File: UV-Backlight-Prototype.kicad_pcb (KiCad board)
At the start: 2 copper layers, 100 x 100 mm, 86 parts, among them J1 Conn_02x08_Odd_Even

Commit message: Progress Update
Changes to PCB:
Adjusted LED placement
Started Test point placement

Changes to schematic:
Test points for VCC and GND for LED strings 1,2,3 deemed redundant and removed.
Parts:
- removed JP1, JP10, JP11, JP12, JP13, JP14, JP15, JP17, JP18, JP19, JP2, JP20, JP21, JP22, JP23, JP3, JP4, JP5, JP6, JP7, JP9: Jumper_2_Open, Resistor_SMD:R_1206_3216Metric_Pad1.30x1.75mm_HandSolder
- JP16: renamed from LEDS 2
- JP24: renamed from LEDS 3
- JP8: renamed from LEDS 1
- moved D21 178.7 mm to (195.1, 95.1), turned to 180 degrees
- moved D14 175.4 mm to (195.1, 80.1), turned to 180 degrees
- moved D7 173.5 mm to (195.1, 65.1), turned to 180 degrees
- moved D20 172.0 mm to (180.1, 95.1), turned to 180 degrees
- moved D13 168.6 mm to (180.1, 80.1), turned to 180 degrees
- moved D6 166.6 mm to (180.1, 65.1), turned to 180 degrees
- moved D19 165.6 mm to (165.1, 95.1), turned to 180 degrees
- moved D12 162.1 mm to (165.1, 80.1), turned to 180 degrees
- moved D5 160.0 mm to (165.1, 65.1), turned to 180 degrees
- moved D18 159.4 mm to (150.1, 95.1), turned to 180 degrees
- moved D11 155.8 mm to (150.1, 80.1), turned to 180 degrees
- moved D17 154.2 mm to (135.1, 95.1), turned to 180 degrees
- moved D4 153.6 mm to (150.1, 65.1), turned to 180 degrees
- moved D10 149.7 mm to (135.1, 80.1), turned to 180 degrees
- moved D16 148.5 mm to (120.1, 95.1), turned to 180 degrees
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
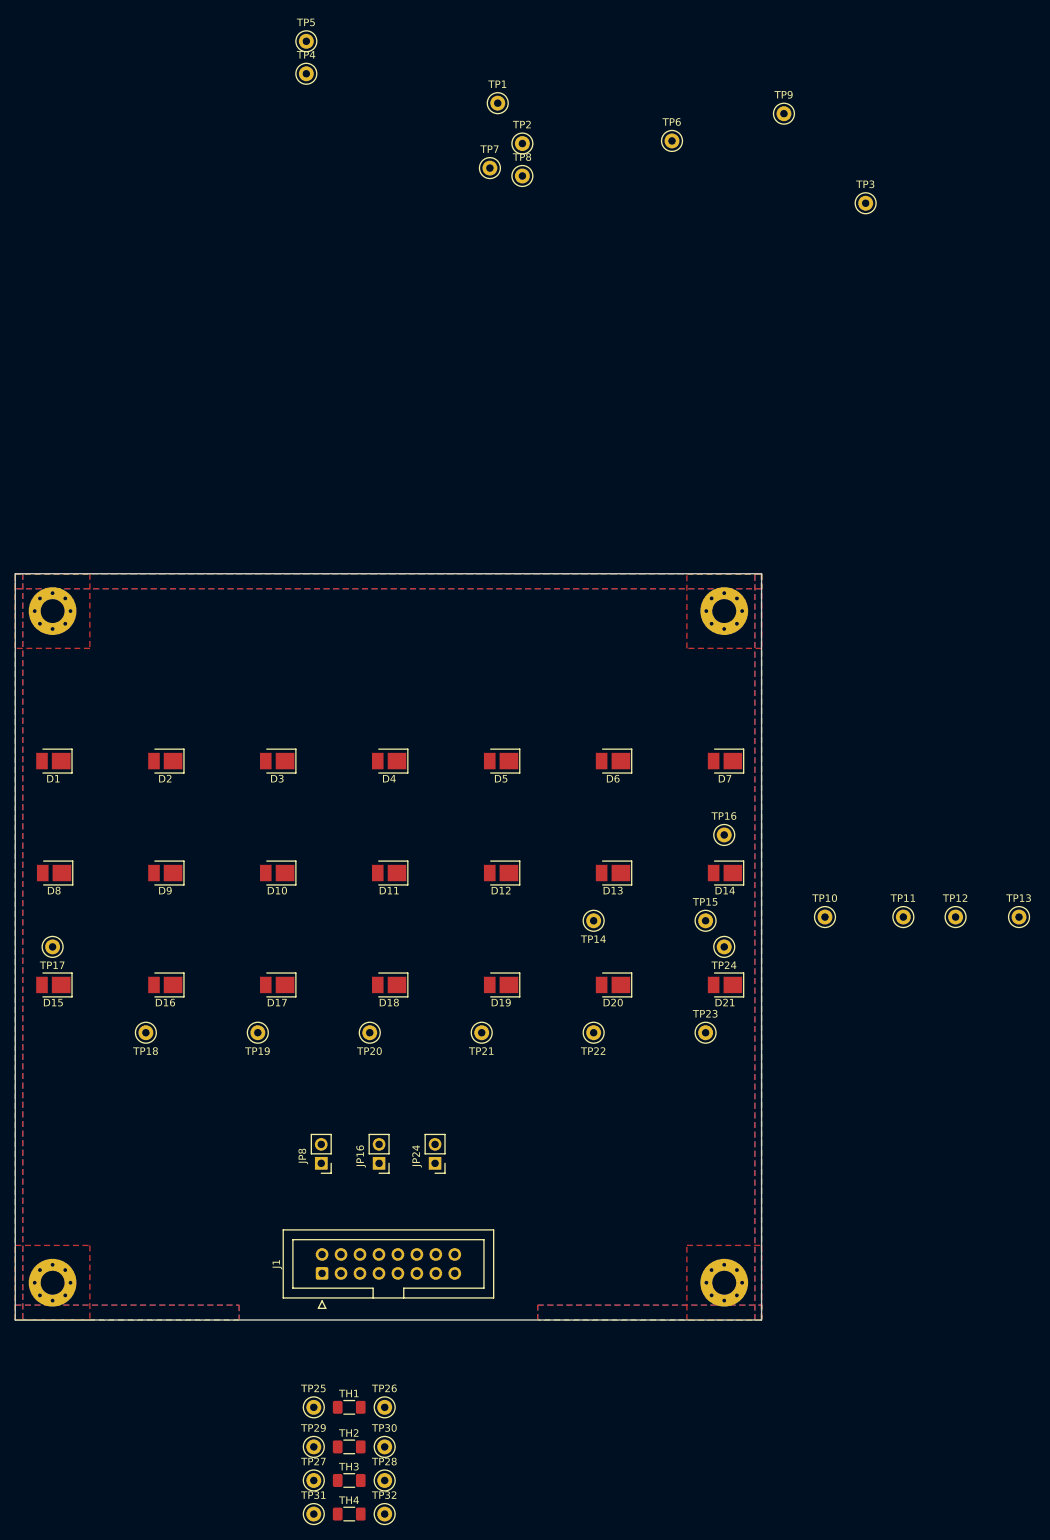
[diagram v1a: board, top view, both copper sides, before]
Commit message: PCB
Component placement complete
Added a section for testpoints for only the thermistors.

Open space bottom right - Add perfboard for prototyping CC drivers
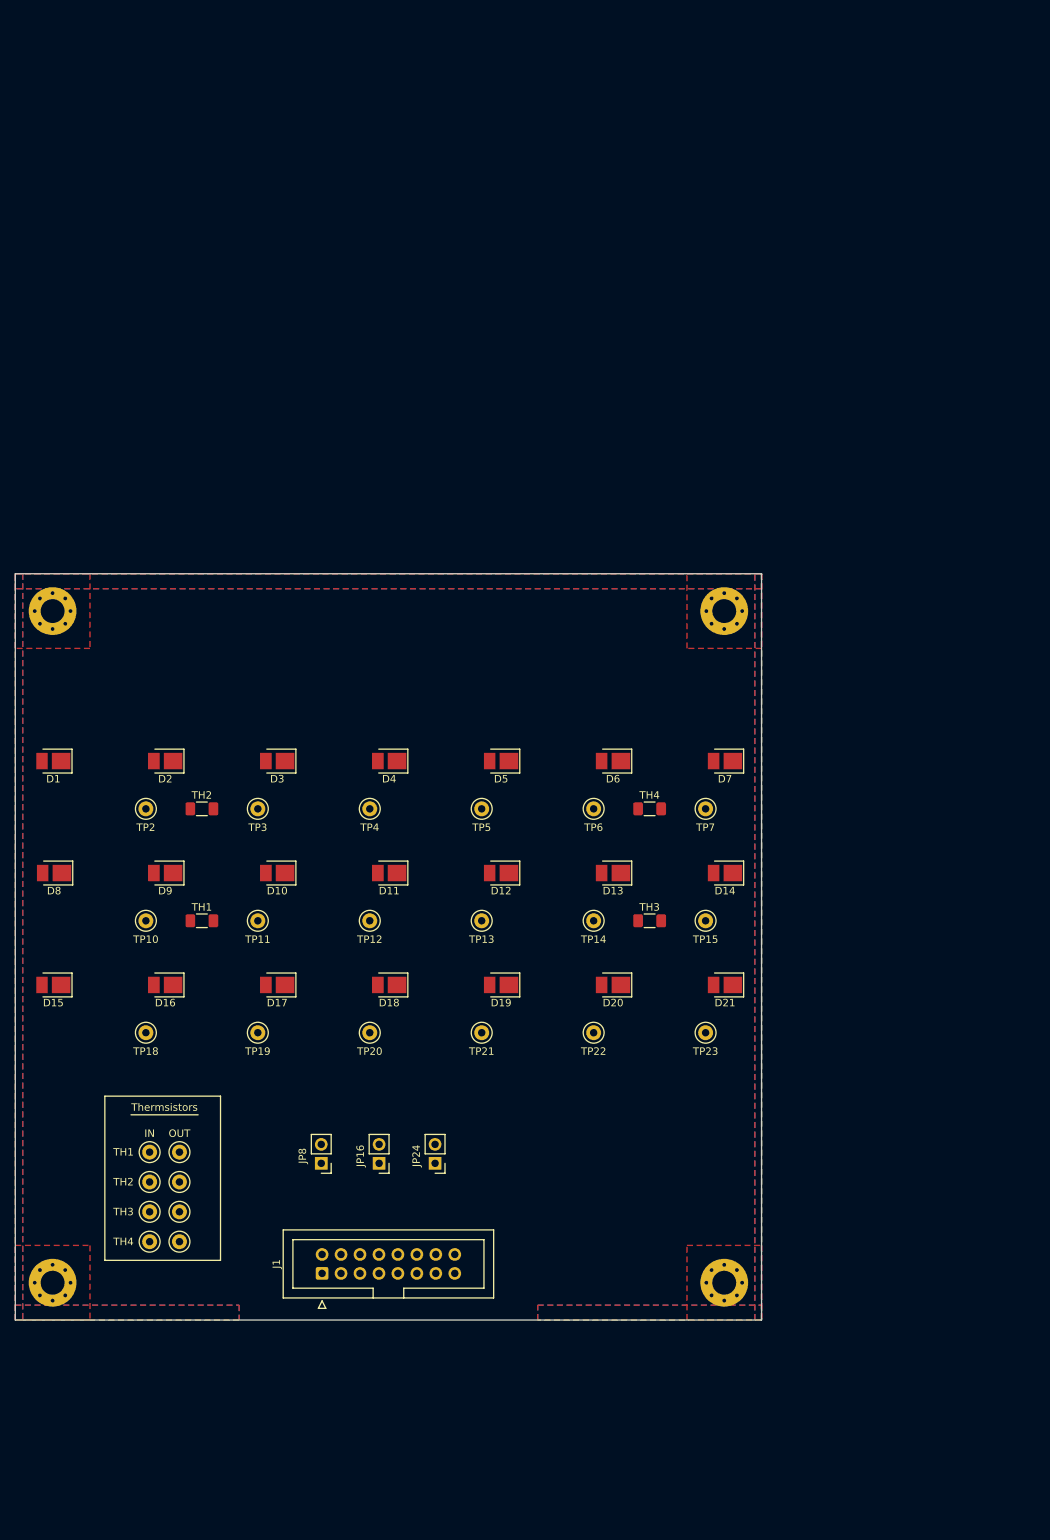
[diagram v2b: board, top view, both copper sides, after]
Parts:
- removed TP1: +LED1, TestPoint:TestPoint_Keystone_5000-5004_Miniature
- removed TP16: -LED14, TestPoint:TestPoint_Keystone_5000-5004_Miniature
- removed TP17: +LED15, TestPoint:TestPoint_Keystone_5000-5004_Miniature
- removed TP24: -LED21, TestPoint:TestPoint_Keystone_5000-5004_Miniature
- removed TP8: -LED7, TestPoint:TestPoint_Keystone_5000-5004_Miniature
- removed TP9: +LED8, TestPoint:TestPoint_Keystone_5000-5004_Miniature
- moved TP3 115.0 mm to (132.5, 71.5)
- moved TP5 105.5 mm to (162.5, 71.5)
- moved TH4 102.7 mm to (185.0, 71.5)
- moved TP2 102.4 mm to (117.5, 71.5)
- moved TP4 98.9 mm to (147.5, 71.5)
- moved TP10 91.0 mm to (117.5, 86.5)
- moved TP7 90.6 mm to (192.5, 71.5)
- moved TP6 90.1 mm to (177.5, 71.5)
- moved TH2 87.8 mm to (125.0, 71.5)
- moved TP11 86.5 mm to (132.5, 86.5)
- moved TH3 85.1 mm to (185.0, 86.5)
- moved TP12 78.5 mm to (147.5, 86.5)
- moved TP13 72.0 mm to (162.5, 86.5)
- moved TH1 68.1 mm to (125.0, 86.5)
- moved TP32 45.7 mm to (122.0, 129.5)
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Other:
- board text added: "IN"
- board text added: "OUT"
- board text added: "TH1"
- board text added: "TH2"
- board text added: "TH3"
- board text added: "TH4"
- board text added: "Thermsistors"

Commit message: Sent to production
PCB created and sent to production for the first prototype
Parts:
- added ?: , clipboard:e0d5eb0a-6c50-48e5-8d74-95606411ad53, F.Cu at (169.5, 112.6)
- added REF**: C_0805_2012Metric_Pad1.18x1.45mm_HandSolder, Capacitor_SMD:C_0805_2012Metric_Pad1.18x1.45mm_HandSolder, F.Cu at (195.5, 118.9)
- added REF**: C_0805_2012Metric_Pad1.18x1.45mm_HandSolder, Capacitor_SMD:C_0805_2012Metric_Pad1.18x1.45mm_HandSolder, F.Cu at (190.4, 118.9)
- added REF**: C_0805_2012Metric_Pad1.18x1.45mm_HandSolder, Capacitor_SMD:C_0805_2012Metric_Pad1.18x1.45mm_HandSolder, F.Cu at (192.9, 113.8)
- added REF**: C_0805_2012Metric_Pad1.18x1.45mm_HandSolder, Capacitor_SMD:C_0805_2012Metric_Pad1.18x1.45mm_HandSolder, F.Cu at (195.9, 113.8)
- added REF**: C_0805_2012Metric_Pad1.18x1.45mm_HandSolder, Capacitor_SMD:C_0805_2012Metric_Pad1.18x1.45mm_HandSolder, F.Cu at (190.2, 113.8)
- added REF**: C_0805_2012Metric_Pad1.18x1.45mm_HandSolder, Capacitor_SMD:C_0805_2012Metric_Pad1.18x1.45mm_HandSolder, F.Cu at (192.8, 118.9)
- added REF**: SOT-89-3_Handsoldering, Package_TO_SOT_SMD:SOT-89-3_Handsoldering, F.Cu at (193.5, 125.2)
- moved TP25 1.50 mm to (116.5, 117.5)
- moved TP26 1.50 mm to (120.5, 117.5)
- moved TP27 1.50 mm to (116.5, 125.5)
- moved TP28 1.50 mm to (120.5, 125.5)
- moved TP29 1.50 mm to (116.5, 121.5)
- moved TP30 1.50 mm to (120.5, 121.5)
- moved TP31 1.50 mm to (116.5, 129.5)
- moved TP32 1.50 mm to (120.5, 129.5)
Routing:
- net T3-In: track 0.00 -> 226.4 mm, vias 0 -> 3
- net T3-Out: track 0.00 -> 224.0 mm, vias 0 -> 2
- net T4-In: track 0.00 -> 210.3 mm, vias 0 -> 3
- net T4-Out: track 0.00 -> 207.1 mm, vias 0 -> 3
- net Net-(D7-Pad1): track 0.00 -> 108.2 mm, vias 0 -> 2
- net T2-In: track 0.00 -> 102.8 mm, vias 0 -> 3
- net VCC-LED1: track 0.00 -> 102.0 mm
- net T2-Out: track 0.00 -> 98.4 mm, vias 0 -> 3
- net (no net): track 0.00 -> 95.5 mm
- net VCC-LED2: track 0.00 -> 94.4 mm
- net VCC-LED3: track 0.00 -> 85.7 mm
- net Net-(D14-Pad1): track 0.00 -> 85.4 mm, vias 0 -> 2
- net T1-In: track 0.00 -> 81.4 mm, vias 0 -> 2
- net T1-Out: track 0.00 -> 80.4 mm, vias 0 -> 2
- net Net-(D21-Pad1): track 0.00 -> 60.0 mm
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- added copper zone on F.Cu, net Net-(D1-Pad1)
- added copper zone on F.Cu, net Net-(D10-Pad1)
- added copper zone on F.Cu, net Net-(D10-Pad2)
- added copper zone on F.Cu, net Net-(D11-Pad1)
- added copper zone on F.Cu, net Net-(D12-Pad1)
- added copper zone on F.Cu, net Net-(D13-Pad1)
- added copper zone on F.Cu, net Net-(D15-Pad1)
- added copper zone on F.Cu, net Net-(D16-Pad1)
- added copper zone on F.Cu, net Net-(D17-Pad1)
- added copper zone on F.Cu, net Net-(D18-Pad1)
- added copper zone on F.Cu, net Net-(D19-Pad1)
- added copper zone on F.Cu, net Net-(D2-Pad1)
- added copper zone on F.Cu, net Net-(D20-Pad1)
- added copper zone on F.Cu, net Net-(D3-Pad1)
- added copper zone on F.Cu, net Net-(D4-Pad1)
- added copper zone on F.Cu, net Net-(D5-Pad1)
- added copper zone on F.Cu, net Net-(D6-Pad1)
- added copper zone on F.Cu, net Net-(D8-Pad1)
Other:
- outline, holes or cut-outs redrawn
